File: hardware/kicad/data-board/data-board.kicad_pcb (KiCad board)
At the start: 4 copper layers, 120 x 90 mm, 144 parts, among them J1 3.3V LoRaWAN, J14 Conn_02x05_Odd_Even, J17 Molex 470531000, J2 3.3V SWARM, J3 BMS I2C, J4 5V RPi CM4, J5 USB_67298-4090, J6 12V Fan, J7 USB_OTG, SW1 Wake, U1 TPD4EUSB30, U10 RAK5146, U11 EMC2301-1-ACZL-TR, U12 Swarm_M138, U13 FSUSB42MUX, U14 74LVC1G07SE-7, U2 TPD4EUSB30, U3 MagJack-A70-112-331N126, U4 TPD4EUSB30, U5 74LVC1G07SE-7, U6 USB2514B_Bi, U7 AP2553W6, U8 PCF85063AT/AAZ, U9 74LVC1G07SE-7, Y1 24MHz, Y2 X32K768S301

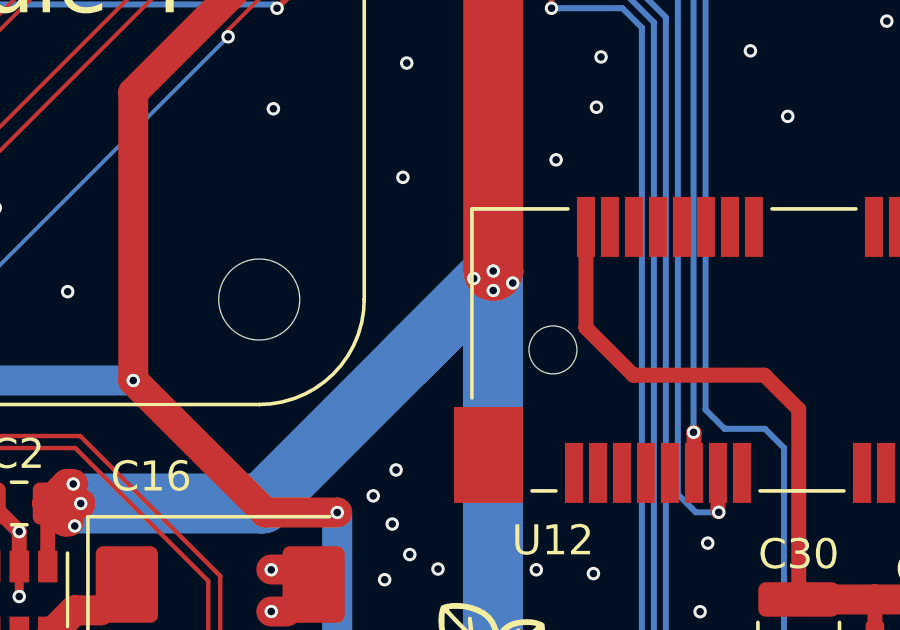
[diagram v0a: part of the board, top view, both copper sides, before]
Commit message: rename to data-board
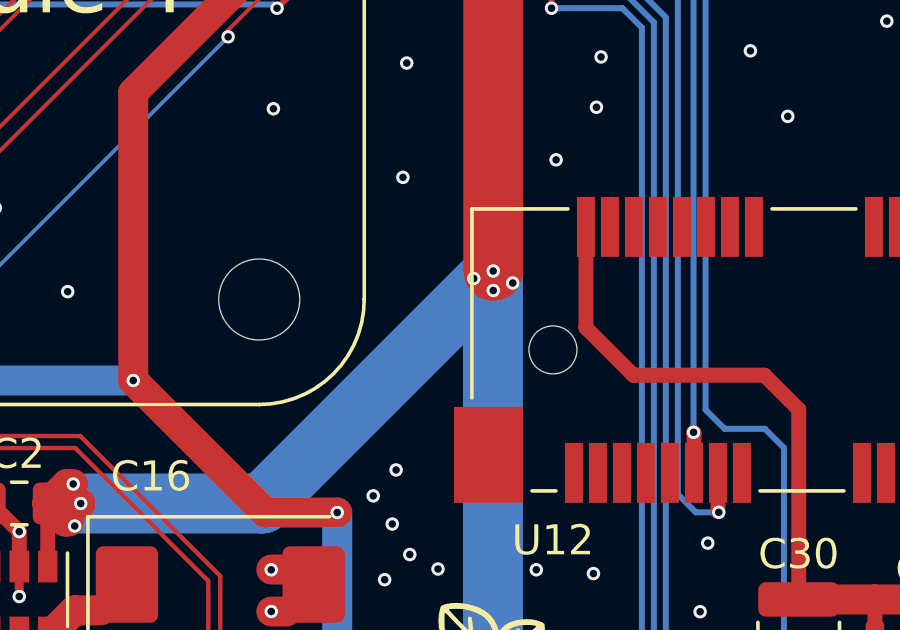
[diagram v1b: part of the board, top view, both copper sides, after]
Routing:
- net /+5v: track 189.3 -> 185.1 mm

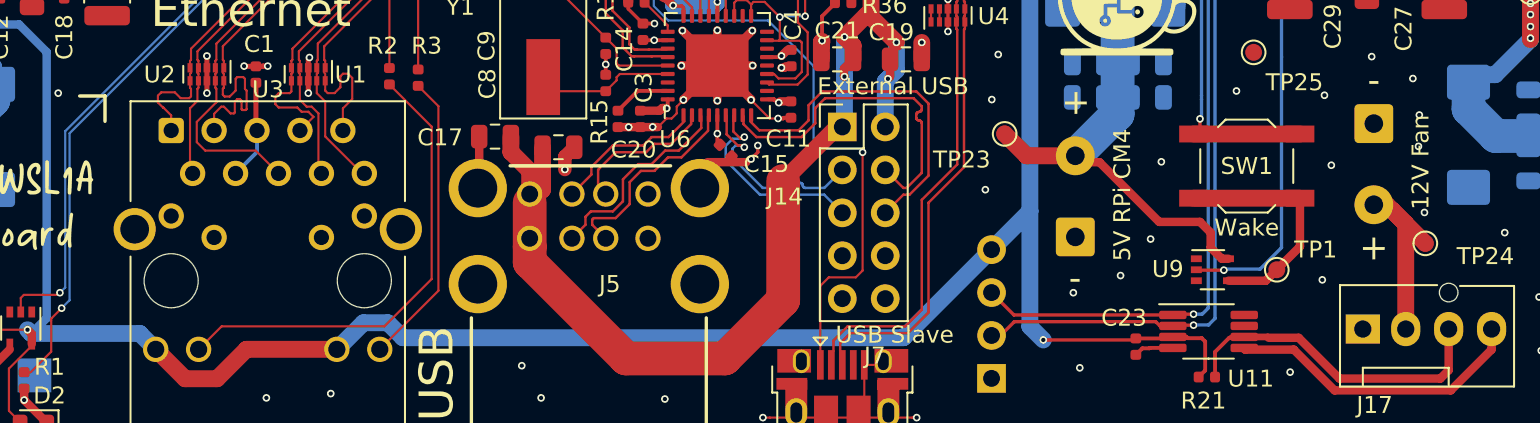
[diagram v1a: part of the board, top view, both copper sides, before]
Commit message: breaks out PoE ttap
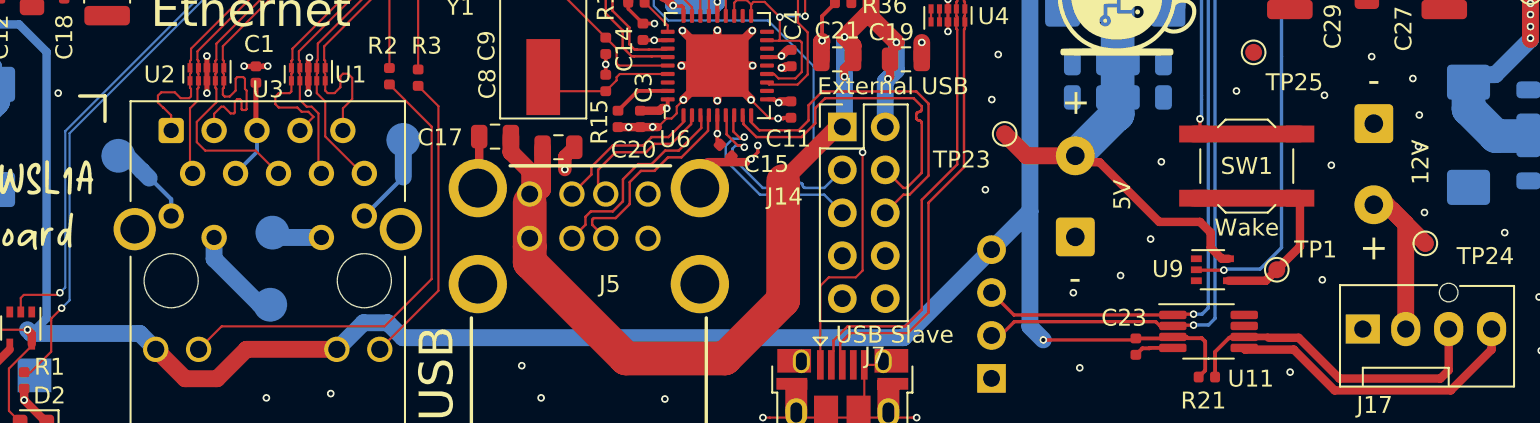
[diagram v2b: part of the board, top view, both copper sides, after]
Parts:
- added TP27: TR0_TAP, TestPoint:TestPoint_Pad_D2.0mm, B.Cu at (110.2, 130.3)
- added TP28: TR1_TAP, TestPoint:TestPoint_Pad_D2.0mm, B.Cu at (119.2, 139.1)
- added TP29: TR2_TAP, TestPoint:TestPoint_Pad_D2.0mm, B.Cu at (119.4, 134.9)
- added TP30: TR3_TAP, TestPoint:TestPoint_Pad_D2.0mm, B.Cu at (127.1, 129.4)
- J4: value 5V RPi CM4 -> 5V
- J6: value 12V Fan -> 12V
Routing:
- net /IO_Ethernet/TR1_TAP: track 0.00 -> 5.71 mm
- net /IO_Ethernet/TR3_TAP: track 0.00 -> 5.46 mm
- net /IO_Ethernet/TR0_TAP: track 0.00 -> 4.81 mm
- net /IO_Ethernet/TR2_TAP: track 0.00 -> 3.02 mm
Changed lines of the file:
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@@
       (effects (font (size 1 1) (thickness 0.15)))
     )
-    (fp_text value "5V RPi CM4" (at 2.4882 2.7796 270) (layer "F.SilkS")
+    (fp_text value "5V" (at 2.4882 2.7796 270) (layer "F.SilkS")
       (effects (font (size 1 1) (thickness 0.15)))
     )
@@
     (descr "Mounting Hole 3mm")
     (tags "mounting hole 3mm")
-    (property "Sheetfile" "bwsl1a.kicad_sch")
+    (property "Sheetfile" "data-board.kicad_sch")
     (property "Sheetname" "")
     (attr exclude_from_pos_files)
@@
       (effects (font (size 1 1) (thickness 0.15)))
     )
-    (fp_text value "12V Fan" (at 2.2854 -2.7686 90) (layer "F.SilkS")
+    (fp_text value "12V" (at 2.2854 -2.7686 90) (layer "F.SilkS")
       (effects (font (size 1 1) (thickness 0.15)))
     )
@@
     (descr "Mounting Hole 3mm")
     (tags "mounting hole 3mm")
-    (property "Sheetfile" "bwsl1a.kicad_sch")
+    (property "Sheetfile" "data-board.kicad_sch")
     (property "Sheetname" "")
     (attr exclude_from_pos_files)
@@
     (descr "Mounting Hole 3mm")
     (tags "mounting hole 3mm")
-    (property "Sheetfile" "bwsl1a.kicad_sch")
+    (property "Sheetfile" "data-board.kicad_sch")
     (property "Sheetname" "")
     (attr exclude_from_pos_files)
@@
     (descr "Mounting Hole 3mm")
     (tags "mounting hole 3mm")
-    (property "Sheetfile" "bwsl1a.kicad_sch")
+    (property "Sheetfile" "data-board.kicad_sch")
     (property "Sheetname" "")
     (attr exclude_from_pos_files)
@@
     )
   )
+  (footprint "TestPoint:TestPoint_Pad_D2.0mm" (layer "B.Cu")
+    (at 110.236 130.3274 180)
+    (descr "SMD pad as test Point, diameter 2.0mm")
+    (tags "test point SMD pad")
+    (property "Sheetfile" "IO_Ethernet.kicad_sch")
+    (property "Sheetname" "IO_Ethernet")
+    (attr exclude_from_pos_files)
+    (fp_text reference "TP27" (at 2.4892 -2.3642) (layer "B.Fab")
+      (effects (font (size 1 1) (thickness 0.15)) (justify mirror))
+    )
+    (fp_text value "TR0_TAP" (at 1.2954 2.1082) (layer "B.Fab")
+      (effects (font (size 1 1) (thickness 0.15)) (justify mirror))
+    )
+    (fp_text user "${REFERENCE}" (at 2.4892 -2.3622) (layer "B.Fab")
+      (effects (font (size 1 1) (thickness 0.15)) (justify mirror))
+    )
+    (fp_circle (center 0 0) (end 0 -1.2) (layer "B.SilkS") (width 0.12) (fill none))
+    (fp_circle (center 0 0) (end 1.5 0) (layer "B.CrtYd") (width 0.05) (fill none))
+    (pad "1" smd circle (at 0 0 180) (size 2 2) (layers "B.Cu" "B.Mask")
+      (net 206 "/IO_Ethernet/TR0_TAP") (pinfunction "1") (pintype "passive"))
+  )
   (footprint "Teapot:TeapotLogo" (layer "B.Cu")
     (at 186.944 92.71 180)
@@
     )
   )
+  (footprint "TestPoint:TestPoint_Pad_D2.0mm" (layer "B.Cu")
+    (at 127.1016 129.3876 180)
+    (descr "SMD pad as test Point, diameter 2.0mm")
+    (tags "test point SMD pad")
+    (property "Sheetfile" "IO_Ethernet.kicad_sch")
+    (property "Sheetname" "IO_Ethernet")
+    (attr exclude_from_pos_files)
+    (fp_text reference "TP30" (at -2.2098 3.7084) (layer "B.Fab")
+      (effects (font (size 1 1) (thickness 0.15)) (justify mirror))
+    )
+    (fp_text value "TR3_TAP" (at -0.9398 2.2606) (layer "B.Fab")
+      (effects (font (size 1 1) (thickness 0.15)) (justify mirror))
+    )
+    (fp_text user "${REFERENCE}" (at -2.2098 3.7084) (layer "B.Fab")
+      (effects (font (size 1 1) (thickness 0.15)) (justify mirror))
+    )
+    (fp_circle (center 0 0) (end 0 -1.2) (layer "B.SilkS") (width 0.12) (fill none))
+    (fp_circle (center 0 0) (end 1.5 0) (layer "B.CrtYd") (width 0.05) (fill none))
+    (pad "1" smd circle (at 0 0 180) (size 2 2) (layers "B.Cu" "B.Mask")
+      (net 209 "/IO_Ethernet/TR3_TAP") (pinfunction "1") (pintype "passive"))
+  )
   (footprint "Teapot:TextLogo_DataBoard" (layer "B.Cu")
     (at 186.055 100.711 180)
@@
       (net 1 "GND") (pinfunction "1") (pintype "passive"))
   )
+  (footprint "TestPoint:TestPoint_Pad_D2.0mm" (layer "B.Cu")
+    (at 119.2276 139.1412 180)
+    (descr "SMD pad as test Point, diameter 2.0mm")
+    (tags "test point SMD pad")
+    (property "Sheetfile" "IO_Ethernet.kicad_sch")
+    (property "Sheetname" "IO_Ethernet")
+    (attr exclude_from_pos_files)
+    (fp_text reference "TP28" (at -0.5334 -2.4892) (layer "B.Fab")
+      (effects (font (size 1 1) (thickness 0.15)) (justify mirror))
+    )
+    (fp_text value "TR1_TAP" (at 0.0254 -4.0132) (layer "B.Fab")
+      (effects (font (size 1 1) (thickness 0.15)) (justify mirror))
+    )
+    (fp_text user "${REFERENCE}" (at -0.5334 -2.4872) (layer "B.Fab")
+      (effects (font (size 1 1) (thickness 0.15)) (justify mirror))
+    )
+    (fp_circle (center 0 0) (end 0 -1.2) (layer "B.SilkS") (width 0.12) (fill none))
+    (fp_circle (center 0 0) (end 1.5 0) (layer "B.CrtYd") (width 0.05) (fill none))
+    (pad "1" smd circle (at 0 0 180) (size 2 2) (layers "B.Cu" "B.Mask")
+      (net 207 "/IO_Ethernet/TR1_TAP") (pinfunction "1") (pintype "passive"))
+  )
   (footprint "TestPoint:TestPoint_Pad_D1.0mm" (layer "B.Cu")
     (at 112.5324 117.3888 90)
@@
       (net 196 "/IO_Ethernet/GLOBAL_EN") (pinfunction "1") (pintype "passive"))
   )
+  (footprint "TestPoint:TestPoint_Pad_D2.0mm" (layer "B.Cu")
+    (at 119.3546 134.874 180)
+    (descr "SMD pad as test Point, diameter 2.0mm")
+    (tags "test point SMD pad")
+    (property "Sheetfile" "IO_Ethernet.kicad_sch")
+    (property "Sheetname" "IO_Ethernet")
+    (attr exclude_from_pos_files)
+    (fp_text reference "TP29" (at -1.8796 -2.2118) (layer "B.Fab")
+      (effects (font (size 1 1) (thickness 0.15)) (justify mirror))
+    )
+    (fp_text value "TR2_TAP" (at -1.524 1.7526) (layer "B.Fab")
+      (effects (font (size 1 1) (thickness 0.15)) (justify mirror))
+    )
+    (fp_text user "${REFERENCE}" (at -1.8796 -2.2098) (layer "B.Fab")
+      (effects (font (size 1 1) (thickness 0.15)) (justify mirror))
+    )
+    (fp_circle (center 0 0) (end 0 -1.2) (layer "B.SilkS") (width 0.12) (fill none))
+    (fp_circle (center 0 0) (end 1.5 0) (layer "B.CrtYd") (width 0.05) (fill none))
+    (pad "1" smd circle (at 0 0 180) (size 2 2) (layers "B.Cu" "B.Mask")
+      (net 208 "/IO_Ethernet/TR2_TAP") (pinfunction "1") (pintype "passive"))
+  )
   (footprint "Capacitor_SMD:C_0805_2012Metric" (layer "B.Cu")
     (at 99.2987 127.9398 90)
@@
   (segment (start 111.2878 116.5252) (end 112.1514 117.3888) (width 0.2) (layer "B.Cu") (net 205))
   (segment (start 112.1514 117.3888) (end 112.5324 117.3888) (width 0.2) (layer "B.Cu") (net 205))
+  (segment (start 110.744 130.3274) (end 111.633 131.2164) (width 1) (layer "B.Cu") (net 206))
+  (segment (start 113.365 132.8976) (end 112.3442 131.8768) (width 0.25) (layer "B.Cu") (net 206))
+  (segment (start 110.236 130.3274) (end 110.744 130.3274) (width 1) (layer "B.Cu") (net 206))
+  (segment (start 111.633 131.2164) (end 112.0648 131.6482) (width 1) (layer "B.Cu") (net 206))
+  (segment (start 113.365 133.89) (end 113.365 132.8976) (width 0.25) (layer "B.Cu") (net 206))
+  (segment (start 115.905 135.16) (end 115.905 136.4282) (width 1) (layer "B.Cu") (net 207))
+  (segment (start 115.905 136.4282) (end 118.618 139.1412) (width 1) (layer "B.Cu") (net 207))
+  (segment (start 118.618 139.1412) (end 119.2276 139.1412) (width 1) (layer "B.Cu") (net 207))
+  (segment (start 119.6406 135.16) (end 119.3546 134.874) (width 1) (layer "B.Cu") (net 208))
+  (segment (start 122.255 135.16) (end 119.6406 135.16) (width 1) (layer "B.Cu") (net 208))
+  (segment (start 127.1016 129.3876) (end 127.1016 131.5834) (width 1) (layer "B.Cu") (net 209))
+  (segment (start 124.795 133.89) (end 127.1016 131.5834) (width 0.25) (layer "B.Cu") (net 209))
   (segment (start 151.78 142.7) (end 151.78 138.02) (width 0.13) (layer "F.Cu") (net 261))
   (segment (start 139.93 115.77) (end 140.33 115.77) (width 0.13) (layer "F.Cu") (net 261))

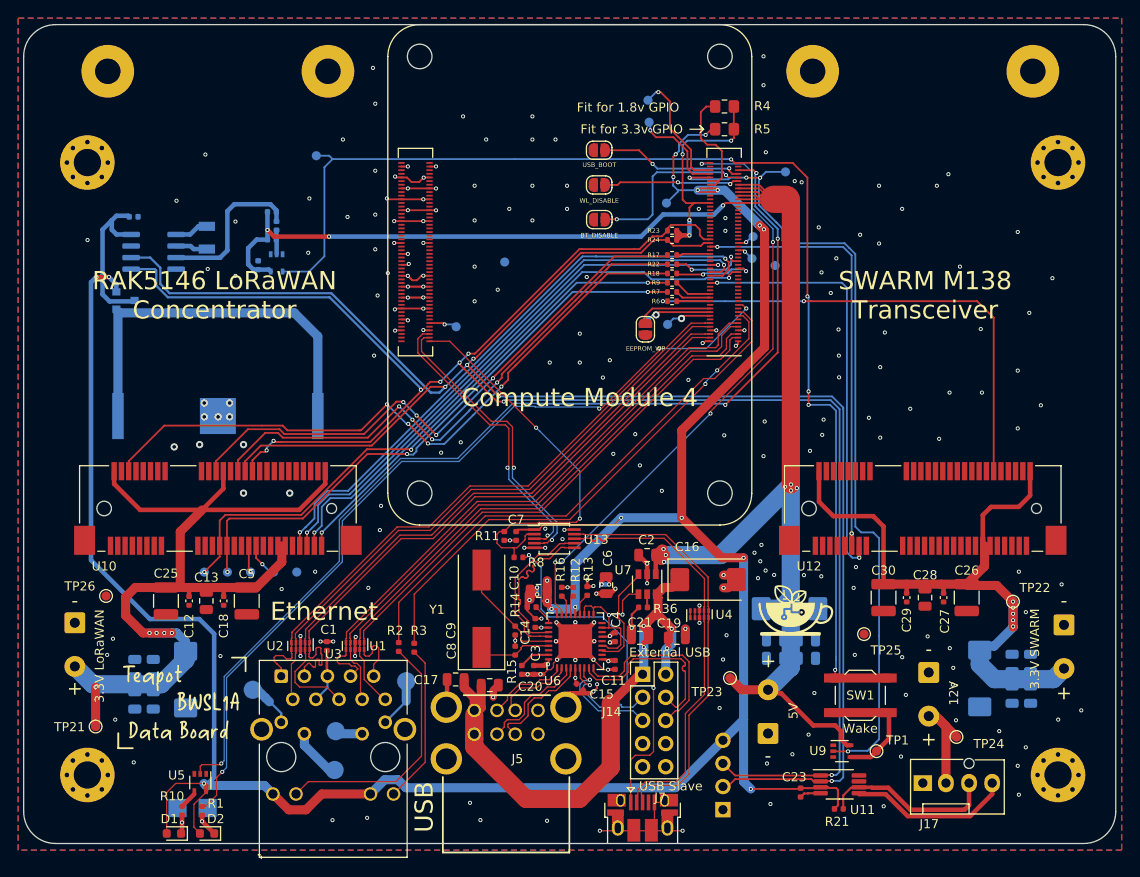
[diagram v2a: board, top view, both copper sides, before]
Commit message: change poe tap location and change debug solder jumper to jst
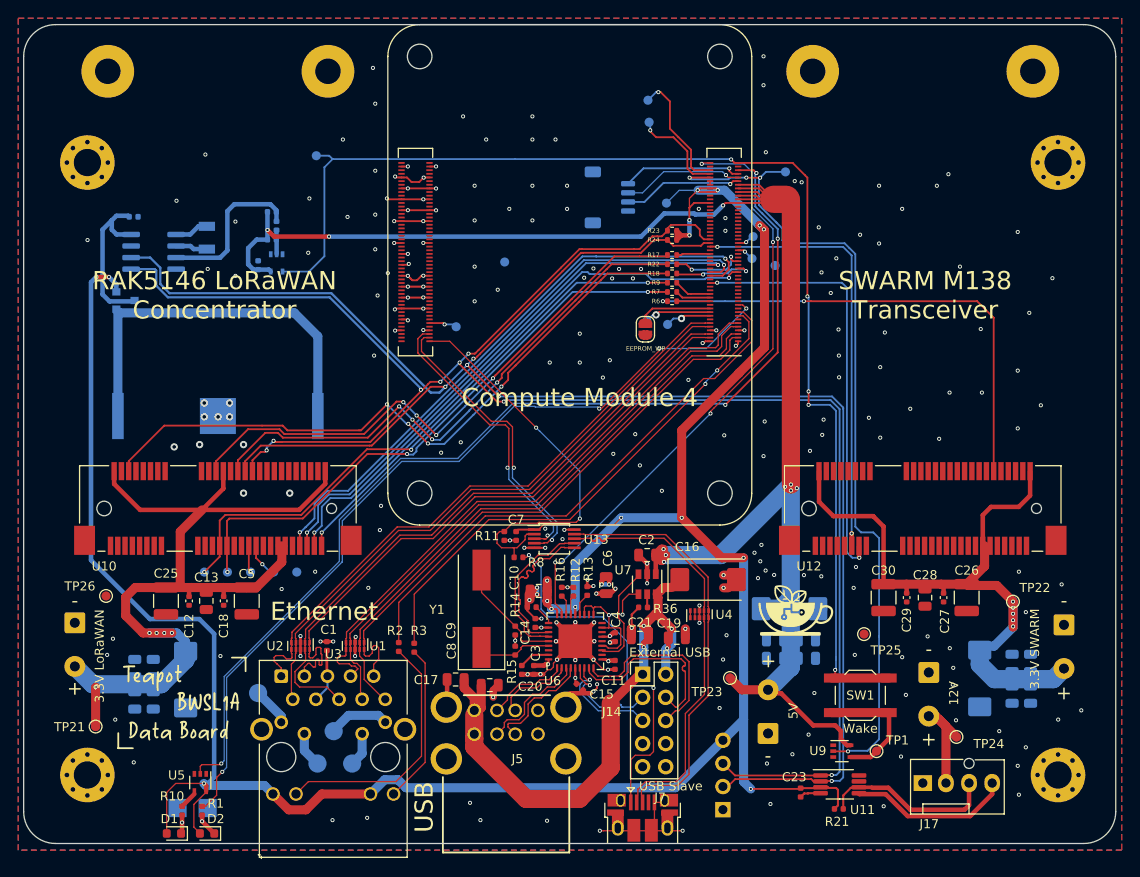
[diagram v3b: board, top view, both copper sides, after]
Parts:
- removed JP1: WL_DISABLE, Jumper:SolderJumper-2_P1.3mm_Open_RoundedPad1.0x1.5mm
- removed JP2: BT_DISABLE, Jumper:SolderJumper-2_P1.3mm_Open_RoundedPad1.0x1.5mm
- removed JP4: USB_BOOT, Jumper:SolderJumper-2_P1.3mm_Open_RoundedPad1.0x1.5mm
- removed R4: nf, Resistor_SMD:R_0805_2012Metric_Pad1.15x1.40mm_HandSolder
- removed R5: 0R, Resistor_SMD:R_0805_2012Metric_Pad1.15x1.40mm_HandSolder
- added J8: Conn_01x04, Connector_JST:JST_SH_SM04B-SRSS-TB_1x04-1MP_P1.00mm_Horizontal, B.Cu at (149.5, 76.2)
- moved TP30 9.68 mm to (119.1, 134.9)
- moved TP29 3.99 mm to (121.2, 138.4)
- moved TP28 2.01 mm to (117.3, 138.4)
- moved TP27 0.68 mm to (110.8, 130.7)
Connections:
- Module1 pad 78: /IO_Ethernet/GPIO_VREF -> /+3.3v
- R23 pad 1: /IO_Ethernet/GPIO_VREF -> /+3.3v
- R24 pad 1: /IO_Ethernet/GPIO_VREF -> /+3.3v
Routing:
- net /IO_Ethernet/GPIO_VREF: track 25.7 -> 0.00 mm, vias 4 -> 0
- net /IO_Ethernet/+1.8v: track 13.1 -> 0.44 mm
- net /IO_Ethernet/BT_nDis: track 19.5 -> 13.3 mm, vias 2 -> 1
- net /IO_Ethernet/nRPIBOOT: track 15.9 -> 13.2 mm, vias 2 -> 1
- net /IO_Ethernet/TR1_TAP: track 5.71 -> 3.61 mm
- net /IO_Ethernet/WL_nDis: track 15.0 -> 13.1 mm, vias 2 -> 1
- net /IO_Ethernet/TR3_TAP: track 5.46 -> 6.66 mm
- net /+3.3v: track 313.9 -> 314.7 mm, vias 25 -> 24
- net /IO_Ethernet/TR2_TAP: track 3.02 -> 3.72 mm
- net /IO_Ethernet/TR0_TAP: track 4.81 -> 4.26 mm
- net GND: vias 229 -> 234
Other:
- board text removed: "Fit for 1.8v GPIO"
- board text removed: "Fit for 3.3v GPIO"
